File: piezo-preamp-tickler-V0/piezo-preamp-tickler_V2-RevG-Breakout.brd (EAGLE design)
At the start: 1.3 x 67.3 mm, 73 parts, among them IC1 OPA2134UA, J1 12V, J10 AUDIO-JACK3LGPADS, J11 AUDIO-JACK3LGPADS, J15 Buf2_BYPASS, J2 12V, J3 Piezo, J4 12V, J5 Buf1_OUT, J6 OpAmp_IN, J7 12V, J8 OpAmp_OUT, J9 Buf2_IN, Q1 J201, Q2 J201SOT-23, Q3 DMN2400, Q4 BQ21040, Q5 SC4503, Q6 BQ297X, SW1 SWITCH_DPDT, SW2 INPUT-select, SW3 SPDT

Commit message: renumbered parts in piezo-preamp-tickler_V2-RevG-Breakout
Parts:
- removed J15: Buf2_BYPASS, SparkFun-Connectors:1X02
- added J14: (no value), SparkFun-Connectors:1X02_LOCK
- J10: value AUDIO-JACK3LGPADS -> Buf2_BYPASS; device Daniel:AUDIO-JACK-TRRS-SMD -> SparkFun-Connectors:1X02
- J12: value (none) -> AUDIO-JACK3LGPADS; device SparkFun-Connectors:USB-B-MICRO-SMD_RED_PASTE -> Daniel:AUDIO-JACK-TRRS-SMD
- J13: device SparkFun-Connectors:1X02_LOCK -> SparkFun-Connectors:USB-B-MICRO-SMD_RED_PASTE
- moved J12 84.7 mm to (83.9, 45.5), turned to 180 degrees
- moved J10 46.5 mm to (49.0, 48.5)
- moved J11 33.7 mm to (83.9, 79.2)
- moved J13 8.95 mm to (2.02, 67.0), turned to 0 degrees
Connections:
- net GND1: now also J13.GND; no longer J12.GND
- net N$11: now also J10.1; no longer J15.1
- net N$12: now also J11.EARTH; no longer J10.EARTH
- net N$13: now also J11.TIP; no longer J10.TIP
- net N$15: now also J11.RING1; no longer J10.RING1
- net N$17: now also J12.EARTH; no longer J11.EARTH
- net N$21: now also J14.2; no longer J13.2
- net N$26: now also J12.RING1; no longer J11.RING1
- net N$27: now also J12.TIP; no longer J11.TIP
- net N$45: now also J12.RING2; no longer J10.RING2
- net N$46: now also J10.2; no longer J15.2
- net V+: now also J13.VBUS; no longer J12.VBUS
- net VBAT: now also J14.1; no longer J13.1
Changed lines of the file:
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@@
 </autorouter>
 <elements>
-<element name="J13" library="SparkFun-Connectors" package="1X02_LOCK" value="" x="2.785" y="75.945" smashed="yes" rot="R90">
+<element name="J14" library="SparkFun-Connectors" package="1X02_LOCK" value="" x="2.785" y="75.945" smashed="yes" rot="R90">
 <attribute name="NAME" x="1.388" y="74.675" size="1.05" layer="25" font="vector" ratio="15" rot="R90"/>
 <attribute name="VALUE" x="4.817" y="74.675" size="0.6096" layer="27" font="vector" ratio="20" rot="R90"/>
@@
 </element>
 <element name="SW2" library="CMU-ArtFab" package="SWITCH_SPDT_CL-SB-12B" value="INPUT-select" x="62.865" y="78.675" smashed="yes" rot="R180"/>
-<element name="J10" library="Daniel" package="AUDIO-JACK-TRRS-SMD" value="AUDIO-JACK3LGPADS" x="83.915" y="79.215" smashed="yes" rot="R180"/>
-<element name="J11" library="Daniel" package="AUDIO-JACK-TRRS-SMD" value="AUDIO-JACK3LGPADS" x="83.915" y="45.515" smashed="yes" rot="R180"/>
+<element name="J11" library="Daniel" package="AUDIO-JACK-TRRS-SMD" value="AUDIO-JACK3LGPADS" x="83.915" y="79.215" smashed="yes" rot="R180"/>
+<element name="J12" library="Daniel" package="AUDIO-JACK-TRRS-SMD" value="AUDIO-JACK3LGPADS" x="83.915" y="45.515" smashed="yes" rot="R180"/>
 <element name="R2" library="CMU-ArtFab" package="R0805" value="10M" x="3.01" y="10.002" smashed="yes" rot="R90">
 <attribute name="NAME" x="4.068" y="13.322" size="1.05" layer="25" font="vector" ratio="15" rot="R180"/>
@@
 <attribute name="VALUE" x="12.95" y="53.755" size="1.05" layer="27" font="vector" ratio="15"/>
 </element>
-<element name="J12" library="SparkFun-Connectors" library_urn="urn:adsk.eagle:library:513" package="USB-B-MICRO-SMD_RED_PASTE" value="" x="2.015" y="67.025" smashed="yes">
+<element name="J13" library="SparkFun-Connectors" library_urn="urn:adsk.eagle:library:513" package="USB-B-MICRO-SMD_RED_PASTE" value="" x="2.015" y="67.025" smashed="yes">
 <attribute name="NAME" x="0.745" y="71.8256" size="1.05" layer="25" font="vector" ratio="15"/>
 <attribute name="PROD_ID" value="CONN-11752" x="2.015" y="67.025" size="1.778" layer="27" display="off"/>
@@
 <attribute name="VALUE" x="70.01" y="53.474" size="1.05" layer="27" font="vector" ratio="15"/>
 </element>
-<element name="J15" library="SparkFun-Connectors" library_urn="urn:adsk.eagle:library:513" package="1X02" value="Buf2_BYPASS" x="48.985" y="48.548" smashed="yes" rot="R180">
+<element name="J10" library="SparkFun-Connectors" library_urn="urn:adsk.eagle:library:513" package="1X02" value="Buf2_BYPASS" x="48.985" y="48.548" smashed="yes" rot="R180">
 <attribute name="NAME" x="48.856" y="51.611" size="1.05" layer="25" font="vector" ratio="15" rot="R180"/>
 <attribute name="VALUE" x="52.859" y="46.73" size="1.05" layer="27" font="vector" ratio="15" rot="R180"/>
@@
 <contactref element="SW1" pad="4"/>
 <contactref element="J9" pad="2"/>
-<contactref element="J15" pad="1"/>
+<contactref element="J10" pad="1"/>
 <wire x1="47.125" y1="80.875" x2="47.125" y2="76.5" width="0.1524" layer="1"/>
 <wire x1="47.125" y1="76.5" x2="47.205" y2="76.475" width="0.1524" layer="1"/>
@@
 </signal>
 <signal name="N$12">
-<contactref element="J10" pad="EARTH"/>
+<contactref element="J11" pad="EARTH"/>
 <contactref element="SW2" pad="P$1"/>
 <wire x1="72.625" y1="80.875" x2="65.365" y2="80.875" width="0.1524" layer="1"/>
@@
 </signal>
 <signal name="N$13">
-<contactref element="J10" pad="TIP"/>
+<contactref element="J11" pad="TIP"/>
 <contactref element="SW1" pad="2"/>
 <wire x1="51.25" y1="78" x2="49.755" y2="76.505" width="0.1524" layer="1"/>
@@
 </signal>
 <signal name="N$15">
-<contactref element="J10" pad="RING1"/>
+<contactref element="J11" pad="RING1"/>
 <contactref element="SW1" pad="5"/>
 <wire x1="51.25" y1="82.375" x2="49.75" y2="80.875" width="0.1524" layer="1"/>
@@
 </signal>
 <signal name="N$17">
-<contactref element="J11" pad="EARTH"/>
+<contactref element="J12" pad="EARTH"/>
 <contactref element="SW2" pad="P$2"/>
 <wire x1="73.5" y1="65.75" x2="62.875" y2="76.375" width="0.1524" layer="1"/>
@@
 </signal>
 <signal name="N$26">
-<contactref element="J11" pad="RING1"/>
+<contactref element="J12" pad="RING1"/>
 <contactref element="SW1" pad="6"/>
 <wire x1="54.375" y1="78.75" x2="52.25" y2="80.875" width="0.1524" layer="1"/>
@@
 </signal>
 <signal name="N$27">
-<contactref element="J11" pad="TIP"/>
+<contactref element="J12" pad="TIP"/>
 <contactref element="SW1" pad="3"/>
 <wire x1="52.25" y1="64.625" x2="52.25" y2="76.375" width="0.1524" layer="1"/>
@@
 <contactref element="R25" pad="2"/>
 <contactref element="R19" pad="2"/>
-<contactref element="J13" pad="1"/>
+<contactref element="J14" pad="1"/>
 <contactref element="Q4" pad="2"/>
 <contactref element="R24" pad="1"/>
@@
 <signal name="N$21">
 <contactref element="SW3" pad="P$1"/>
-<contactref element="J13" pad="2"/>
+<contactref element="J14" pad="2"/>
 <wire x1="18.125" y1="85.375" x2="22.125" y2="85.375" width="0.1524" layer="1"/>
 <wire x1="18.125" y1="86.125" x2="18.125" y2="85.375" width="0.1524" layer="1"/>
@@
 <signal name="V+">
 <contactref element="LED1" pad="A"/>
-<contactref element="J12" pad="VBUS"/>
+<contactref element="J13" pad="VBUS"/>
 <contactref element="Q4" pad="6"/>
 <contactref element="C10" pad="1"/>
@@
 <contactref element="C10" pad="2"/>
 <contactref element="Q4" pad="5"/>
-<contactref element="J12" pad="GND"/>
+<contactref element="J13" pad="GND"/>
 <contactref element="R18" pad="1"/>
 <contactref element="R21" pad="1"/>
@@
 <contactref element="R15" pad="1"/>
 <contactref element="D5" pad="C"/>
+<contactref element="J12" pad="RING2"/>
 <contactref element="J11" pad="RING2"/>
-<contactref element="J10" pad="RING2"/>
 <contactref element="R13" pad="1"/>
 <contactref element="J9" pad="1"/>
@@
 <contactref element="R13" pad="2"/>
 <contactref element="R14" pad="2"/>
-<contactref element="J15" pad="2"/>
+<contactref element="J10" pad="2"/>
 <wire x1="46.5" y1="48.5" x2="46.5" y2="39.625" width="0.1524" layer="1"/>
 <wire x1="46.5" y1="39.625" x2="46.381" y2="39.526" width="0.1524" layer="1"/>

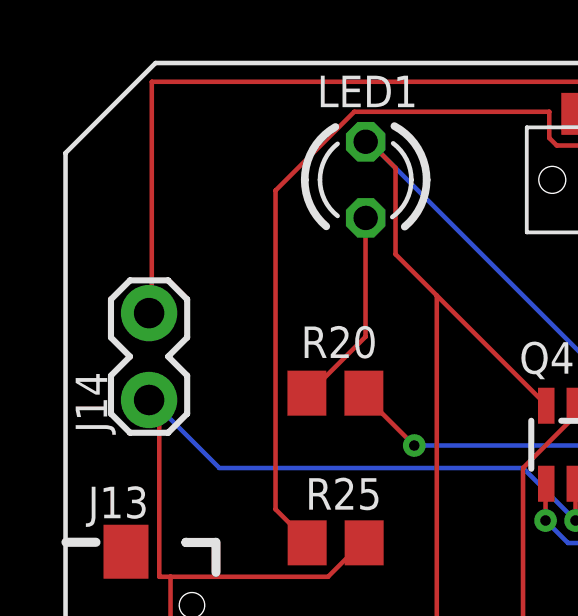
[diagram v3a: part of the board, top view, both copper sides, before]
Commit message: renumbered parts in piezo-preamp-tickler_V2-RevG-Breakout
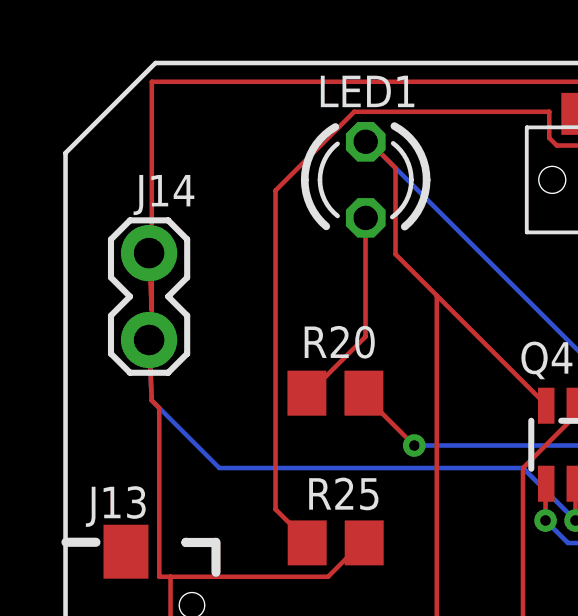
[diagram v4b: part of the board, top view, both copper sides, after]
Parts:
- J14: value (none) -> Battery
- moved J14 2.00 mm to (2.79, 77.9)
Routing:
- net VBAT: track 102.9 -> 106.7 mm
- net N$21: track 27.9 -> 29.7 mm
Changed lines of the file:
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@@
 </autorouter>
 <elements>
-<element name="J14" library="SparkFun-Connectors" package="1X02_LOCK" value="" x="2.785" y="75.945" smashed="yes" rot="R90">
-<attribute name="NAME" x="1.388" y="74.675" size="1.05" layer="25" font="vector" ratio="15" rot="R90"/>
-<attribute name="VALUE" x="4.817" y="74.675" size="0.6096" layer="27" font="vector" ratio="20" rot="R90"/>
+<element name="J14" library="SparkFun-Connectors" package="1X02_LOCK" value="Battery" x="2.785" y="77.945" smashed="yes" rot="R90">
+<attribute name="G" value="-" x="5.531" y="80.216" size="1.5" layer="27" font="vector" ratio="15" rot="R90"/>
+<attribute name="NAME" x="4.366" y="83.269" size="1.05" layer="25" font="vector" ratio="15" rot="R180"/>
+<attribute name="V" value="+" x="5.696" y="77.424" size="1.5" layer="27" font="vector" ratio="15" rot="R90"/>
+<attribute name="VALUE" x="6.231" y="76.529" size="1.05" layer="27" font="vector" ratio="20" rot="R180"/>
 </element>
 <element name="C7" library="adafruit" package="CT7343" value="47uF" x="82.845" y="13.865" smashed="yes" rot="R270">
@@
 <wire x1="2.875" y1="75.75" x2="5.125" y2="73.5" width="0.1524" layer="16"/>
 <wire x1="17" y1="72.875" x2="16.975" y2="72.9749" width="0.1524" layer="1"/>
-<wire x1="2.875" y1="75.75" x2="2.785" y2="75.7672" width="0.1524" layer="16"/>
+<wire x1="2.875" y1="75.75" x2="2.785" y2="77.7672" width="0.1524" layer="16"/>
 <wire x1="8.75" y1="69.875" x2="9.875" y2="71" width="0.1524" layer="1"/>
 <wire x1="3.125" y1="69.875" x2="3.5" y2="69.875" width="0.1524" layer="1"/>
@@
 <wire x1="2.875" y1="75.75" x2="3.125" y2="75.5" width="0.1524" layer="1"/>
 <wire x1="9.875" y1="71" x2="9.955" y2="71.005" width="0.1524" layer="1"/>
-<wire x1="2.875" y1="75.75" x2="2.785" y2="75.7672" width="0.1524" layer="1"/>
+<wire x1="2.875" y1="75.75" x2="2.785" y2="77.7672" width="0.1524" layer="1"/>
 <wire x1="27.25" y1="71" x2="33" y2="71" width="0.1524" layer="1"/>
 <wire x1="20.875" y1="71" x2="27.25" y2="71" width="0.1524" layer="16"/>
@@
 <wire x1="2.875" y1="78.75" x2="2.875" y2="86.375" width="0.1524" layer="1"/>
 <wire x1="22.125" y1="85.375" x2="22.125" y2="85.305" width="0.1524" layer="1"/>
-<wire x1="2.875" y1="78.75" x2="2.785" y2="78.6628" width="0.1524" layer="1"/>
+<wire x1="2.875" y1="78.75" x2="2.785" y2="80.6628" width="0.1524" layer="1"/>
 </signal>
 <signal name="N$31">

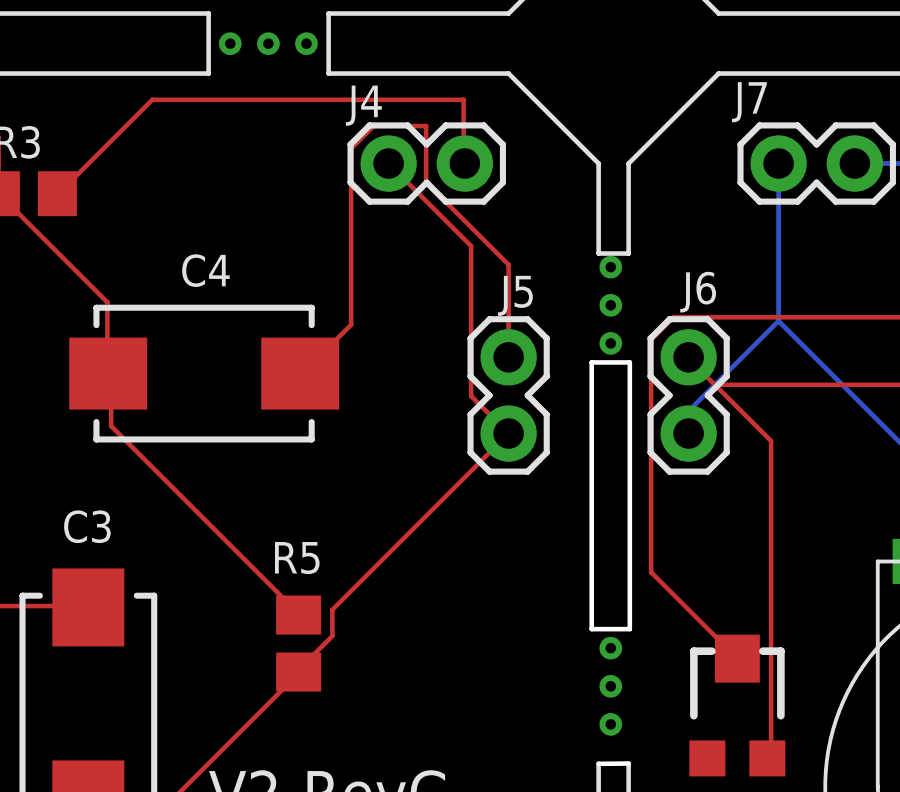
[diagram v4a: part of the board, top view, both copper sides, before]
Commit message: piezo-preamp-tickler_V2-RevG-Breakout routed and GERBER-ed
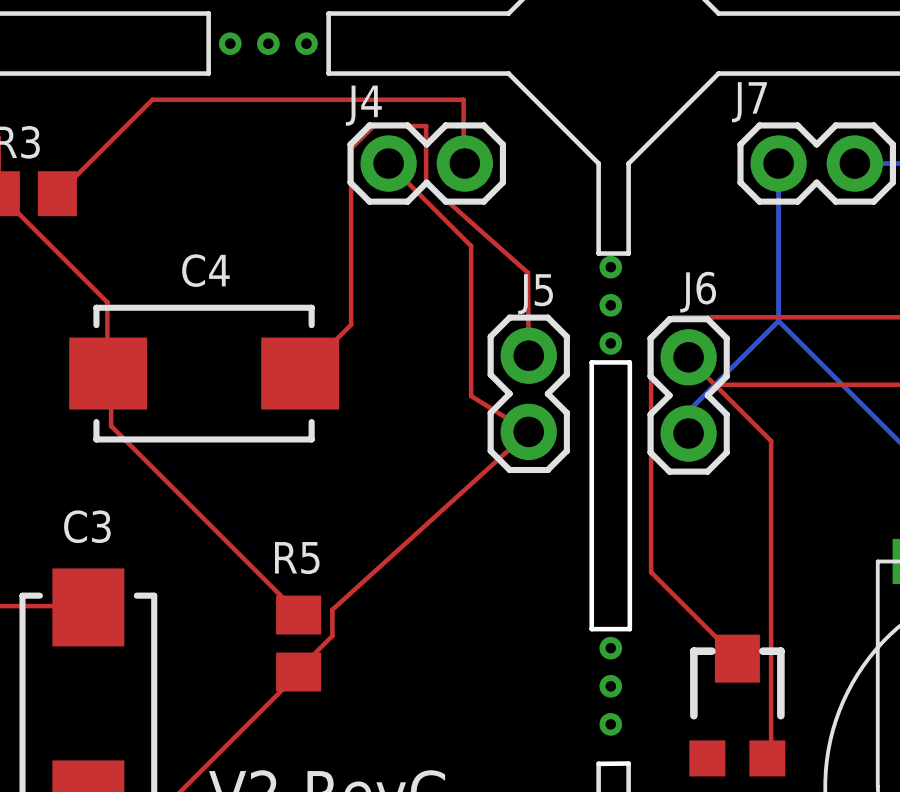
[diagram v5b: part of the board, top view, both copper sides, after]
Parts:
- moved J5 0.67 mm to (36.7, 16.1)
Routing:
- net N$20: track 67.0 -> 68.1 mm
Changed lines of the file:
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@@
 <?xml version="1.0" encoding="utf-8"?>
 <!DOCTYPE eagle SYSTEM "eagle.dtd">
-<eagle version="8.2.2">
+<eagle version="8.3.2">
 <drawing>
 <settings>
 <setting alwaysvectorfont="no"/>
+<setting keepoldvectorfont="yes"/>
 <setting verticaltext="up"/>
 </settings>
@@
 <attribute name="VALUE" x="46.834" y="22.153" size="1.05" layer="27" font="vector" ratio="20"/>
 </element>
-<element name="J5" library="SparkFun-Connectors" library_urn="urn:adsk.eagle:library:513" package="1X02" value="Buf1_OUT" x="36" y="16" smashed="yes" rot="R90">
-<attribute name="NAME" x="36.921" y="21.258" size="1.05" layer="25" font="vector" ratio="15" rot="R180"/>
-<attribute name="VALUE" x="31.419" y="13.06" size="1.05" layer="27" font="vector" ratio="15"/>
+<element name="J5" library="SparkFun-Connectors" library_urn="urn:adsk.eagle:library:513" package="1X02" value="Buf1_OUT" x="36.671" y="16.054" smashed="yes" rot="R90">
+<attribute name="NAME" x="37.592" y="21.312" size="1.05" layer="25" font="vector" ratio="15" rot="R180"/>
+<attribute name="VALUE" x="32.09" y="13.114" size="1.05" layer="27" font="vector" ratio="15"/>
 </element>
 <element name="J6" library="SparkFun-Connectors" library_urn="urn:adsk.eagle:library:513" package="1X02" value="OpAmp_IN" x="42" y="16" smashed="yes" rot="R90">
@@
 <wire x1="33.25" y1="26.25" x2="31.5" y2="26.25" width="0.1524" layer="1"/>
 <wire x1="33.25" y1="24.375" x2="33.25" y2="26.25" width="0.1524" layer="1"/>
-<wire x1="36" y1="21.625" x2="33.25" y2="24.375" width="0.1524" layer="1"/>
-<wire x1="36" y1="18.54" x2="36" y2="21.625" width="0.1524" layer="1"/>
+<wire x1="36.644" y1="21.357" x2="33.25" y2="24.375" width="0.1524" layer="1"/>
+<wire x1="36.671" y1="18.594" x2="36.644" y2="21.357" width="0.1524" layer="1"/>
 <wire x1="29.125" y1="18" x2="29.053" y2="17.998" width="0.1524" layer="1"/>
 </signal>
@@
 <wire x1="34.75" y1="22.25" x2="32" y2="25" width="0.1524" layer="1"/>
 <wire x1="34.75" y1="17.25" x2="34.75" y2="22.25" width="0.1524" layer="1"/>
-<wire x1="36" y1="16" x2="34.75" y2="17.25" width="0.1524" layer="1"/>
+<wire x1="36.671" y1="16.054" x2="34.75" y2="17.25" width="0.1524" layer="1"/>
 <wire x1="24.875" y1="3.875" x2="29" y2="8" width="0.1524" layer="1"/>
 <wire x1="22" y1="3.875" x2="24.875" y2="3.875" width="0.1524" layer="1"/>
@@
 <wire x1="15" y1="4.125" x2="15" y2="3.875" width="0.1524" layer="1"/>
 <wire x1="21.875" y1="3.875" x2="21.991" y2="3.803" width="0.1524" layer="1"/>
-<wire x1="30.125" y1="10.125" x2="36" y2="16" width="0.1524" layer="1"/>
+<wire x1="30.125" y1="10.125" x2="36.671" y2="16.054" width="0.1524" layer="1"/>
 <wire x1="30.125" y1="9.25" x2="30.125" y2="10.125" width="0.1524" layer="1"/>
 <wire x1="29" y1="8.125" x2="30.125" y2="9.25" width="0.1524" layer="1"/>
@@
 </note>
 <note version="8.2" severity="warning">
-Since Version 8.2, Eagle supports online libraries. The ids
+Since Version 8.2, EAGLE supports online libraries. The ids
 of those online libraries will not be understood (or retained)
 with this version.
